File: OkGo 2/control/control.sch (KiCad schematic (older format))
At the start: 40 parts

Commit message: Specced/valued/footprinted a lot of parts
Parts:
- removed C?: CP, symbol CP
- removed C? (x2): C, symbol C
- removed U?: APE8865N-33-HF-3, SOT-23, symbol APE8865N-33-HF-3
- added C103, C104, C106, C114: 100n, Capacitors_SMD:C_0805_HandSoldering, symbol C
- added C113: 100u, Capacitors_SMD:C_1206_HandSoldering, symbol C
- added U101: ADP3335, Housings_SSOP:MSOP-8_3x3mm_Pitch0.65mm, symbol ADP3335
- C101, C102: renamed from C?; value C -> 2u2; footprint (none) -> Capacitors_SMD:C_0805_HandSoldering; Farnell (none) -> 2362106
- C105: renamed from C?; value 100n -> 4u7; footprint (none) -> Capacitors_SMD:C_0805_HandSoldering; Farnell (none) -> 1845742
- C107: renamed from C?; value C -> 100n; footprint (none) -> Capacitors_SMD:C_0805_HandSoldering; Farnell (none) -> 2407344
- C108: renamed from C?; value C -> 4u7; footprint (none) -> Capacitors_SMD:C_0805_HandSoldering; Farnell (none) -> 1845742
- C109: renamed from C?; value C -> 10n; footprint (none) -> Capacitors_SMD:C_0805_HandSoldering; Farnell (none) -> 2407341
- C110: renamed from C?; value C -> 1u; footprint (none) -> Capacitors_SMD:C_0805_HandSoldering; Farnell (none) -> 9227792
- C111, C112: renamed from C?; value C -> 15p; footprint (none) -> Capacitors_SMD:C_0805_HandSoldering; Farnell (none) -> 1414668
- R101: renamed from R?; value R -> 3k3; footprint (none) -> Resistors_SMD:R_0805_HandSoldering; Farnell (none) -> 9237682
- R102: renamed from R?; value R -> 10k; footprint (none) -> Capacitors_SMD:C_0805_HandSoldering; Farnell (none) -> 9237755
- R104, R106, R107, R108: renamed from R?; footprint (none) -> Resistors_SMD:R_0805_HandSoldering; Farnell (none) -> 2331808
- R105: renamed from R?; value R -> 100R; footprint (none) -> Resistors_SMD:R_0805_HandSoldering; Farnell (none) -> 2331783
- RV101: renamed from RV?; Farnell (none) -> 9354824
- U102: renamed from U?; footprint (none) -> common:FTSH-105-01-F-D-K
- U104: renamed from U?; footprint (none) -> Housings_QFP:LQFP-48_7x7mm_Pitch0.5mm; Farnell (none) -> 2432093
- Y101: renamed from Y?; value Crystal -> 8MHz; Farnell (none) -> 2101329
- gave numbers to parts that had none: 16
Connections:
- wire segments 130 -> 147
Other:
- moved on the sheet: C101, C102, D101, P101, R101, R102, R103, TP101, TP102, TP103

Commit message: Lots and lots of part selections and small mods
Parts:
- removed P102, P103, P104, P106: CONN_01X04, symbol CONN_01X04
- removed P105: ANT, symbol CONN_01X02
- removed R104, R106, R107, R108: 10k, Resistors_SMD:R_0805_HandSoldering, symbol R
- added BT?: LiPO_1S, symbol LiPO_1S
- added F?: FUSE, symbol FUSE
- added P?: SMA, common:SMA-142-0701-801, symbol SMA
- added P? (x2): BATT_CASE, symbol CONN_01X02
- added P?: BATT, symbol CONN_01X02
- added P?: BATT_JST_XH, symbol CONN_01X02
- added SW?: Latching Push, symbol SPST_small
- added U?: MEU1S0303ZC, symbol MEU1S0303ZC
- P101: value BATT_IN -> BATT
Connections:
- net labels added: +5V
- wire segments 147 -> 137
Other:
- moved on the sheet: C101, C102, C103, C104, C105, C106, C107, C108, C109, C110, C111, C112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

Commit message: New power buttons and arm/disarm LED
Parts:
- removed P101, P?: BATT, symbol CONN_01X02
- removed SW?: Latching Push, symbol SPST_small
- added D?: Led_x2, symbol Led_x2
- added P? (x2): KEYSW, symbol CONN_01X02
- added P? (x2): BATT, symbol CONN_01X02
- added R?: 10k, Resistors_SMD:R_0805_HandSoldering, symbol R
- added R? (x2): 68R, Resistors_SMD:R_0805_HandSoldering, symbol R
- added SW?: KEYSWITCH, symbol SPST_small
- added SW?: LATCHING PUSH, symbol SPST_small
- added U?: BEZEL, symbol PART
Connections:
- net labels added: +3.3V, ARM_LED, ARM_SW, DISARM_LED
- wire segments 137 -> 153
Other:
- note added: "GREEN: 2.1V 20mA"
- note added: "RED: 1.95V 20mA"
- moved on the sheet: BT?, D101, F?, P?, R101, R102, TP102, TP103

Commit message: Lots of footprinting.
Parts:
- removed D102: POWER, symbol LED
- removed R103: R, symbol R
- added U?: FUSE 1A, symbol PART
- BT101: renamed from BT?; URL (none) -> https://www.coolcomponents.co.uk/lithium-polymer-battery-20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
- F101: renamed from F?; value FUSE -> 5x20; footprint (none) -> control:5x20_clip; Farnell (none) -> 1162740
- RV101: footprint (none) -> control:bourns3386G
- U103: footprint (none) -> Pin_Headers:Pin_Header_Straight_1x16
- U105: footprint (none) -> common:RFM95W
- U106: renamed from U?; footprint (none) -> control:meu1
- Y101: footprint (none) -> common:XTAL50x32
- gave numbers to parts that had none: 15
- renumbered R102 to R103, R105 to R106, TP102 to TP101, TP101 to TP102, U102 to U107
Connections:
- wire segments 153 -> 151
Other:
- moved on the sheet: TP102

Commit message: Finished footprinting control, #7
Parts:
- added P108, P109: ARM_LED, symbol CONN_01X03
- D102: value Led_x2 -> RED/GREEN
- P103: footprint (none) -> common:JST-PA-2; Farnell (none) -> 1830747
- gave numbers to parts that had none: 1
- renumbered P108 to P110, U101 to U102, U102 to U103, U103 to U104, U104 to U105, U105 to U106, U106 to U107, U107 to U108
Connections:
- net GND: now also P108.1 (P1); no longer D102.2 (K)
- net at D102.1 (A1): now also P109.2 (P2); no longer R105.1
- net at D102.3 (A2): now also P109.3 (P3); no longer R104.1
- new net: D102.2 (K), P109.1 (P1)
- new net: P108.3 (P3), R104.1
- new net: P108.2 (P2), R105.1
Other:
- moved on the sheet: D102, R104, U103

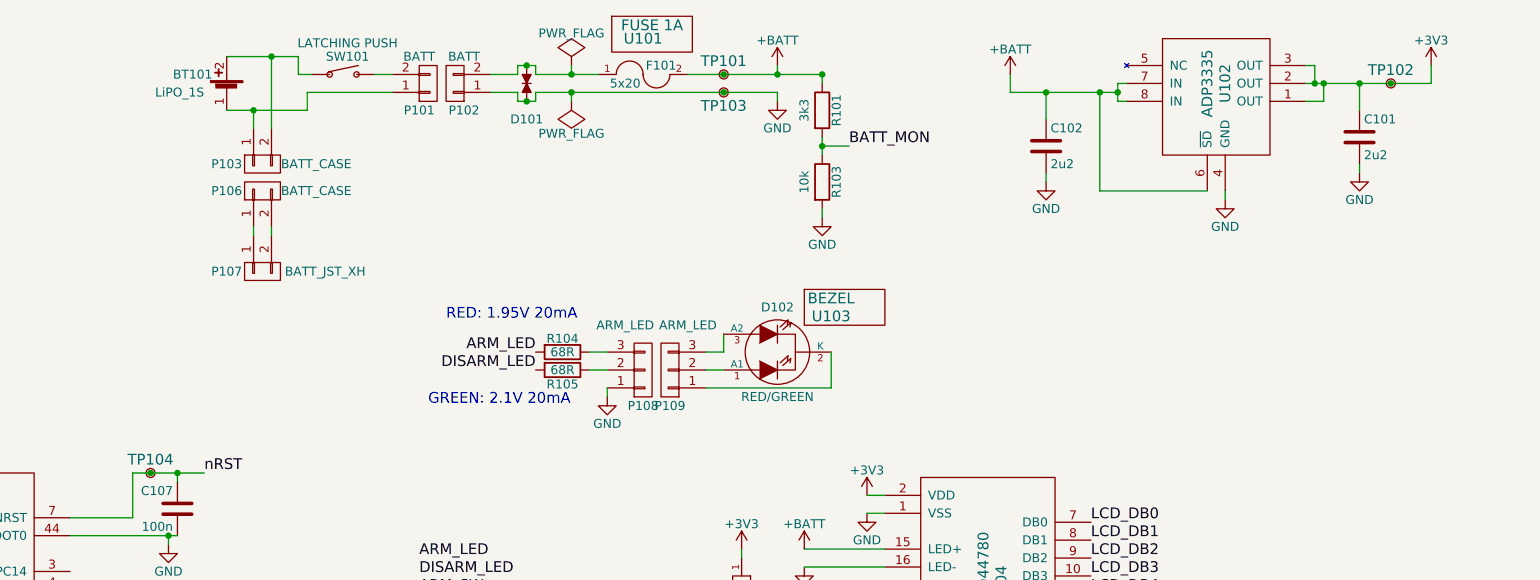
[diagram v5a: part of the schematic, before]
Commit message: Footprinting on ignition + TPs
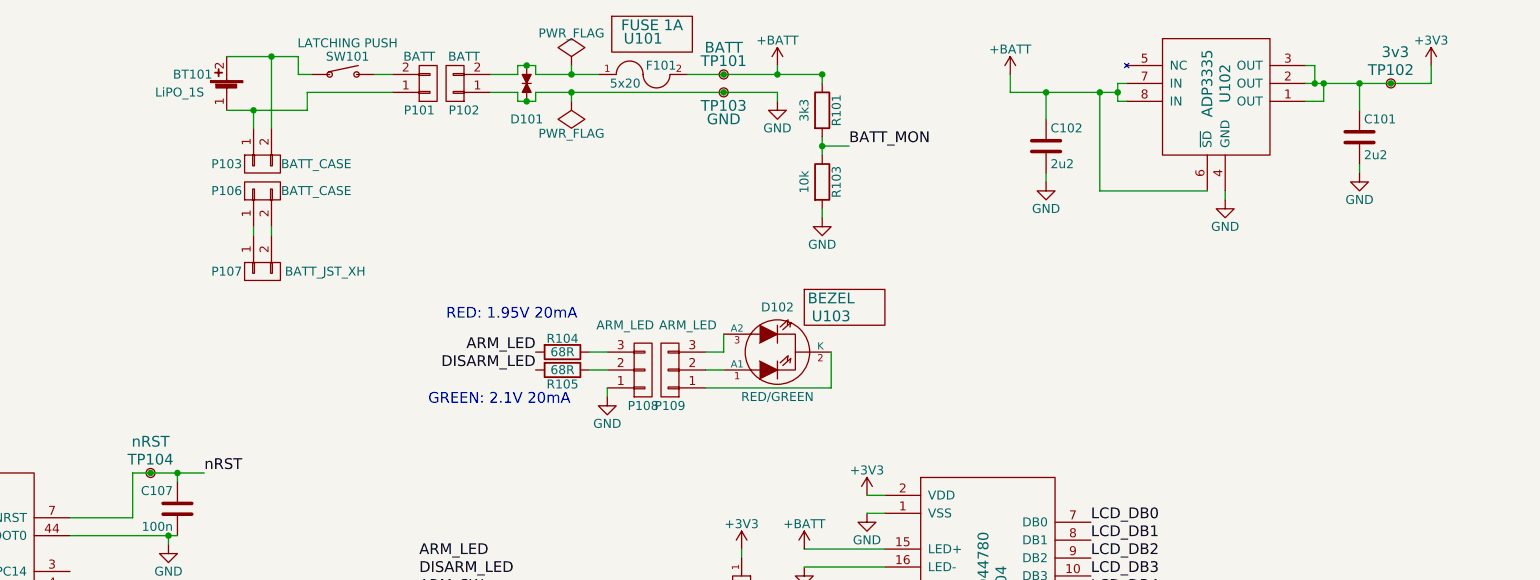
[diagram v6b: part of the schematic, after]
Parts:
- TP101: value TestPoint -> BATT; footprint (none) -> common:TESTPOINT
- TP102: value TestPoint -> 3v3; footprint (none) -> common:TESTPOINT
- TP103: value TestPoint -> GND; footprint (none) -> common:TESTPOINT
- TP104: value TestPoint -> nRST; footprint (none) -> common:TESTPOINT
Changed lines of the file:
@@
 P 10425 950
 F 0 "TP102" H 10425 875 60  0000 C CNN
-F 1 "TestPoint" H 10400 775 60  0001 C CNN
-F 2 "" H 10425 950 60  0000 C CNN
+F 1 "3v3" H 10400 775 60  0000 C CNN
+F 2 "common:TESTPOINT" H 10425 950 60  0001 C CNN
 F 3 "" H 10425 950 60  0000 C CNN
 	1    10425 950
@@
 P 6700 900
 F 0 "TP101" H 6700 825 60  0000 C CNN
-F 1 "TestPoint" H 6675 725 60  0001 C CNN
-F 2 "" H 6700 900 60  0000 C CNN
+F 1 "BATT" H 6700 750 60  0000 C CNN
+F 2 "common:TESTPOINT" H 6700 900 60  0001 C CNN
 F 3 "" H 6700 900 60  0000 C CNN
 	1    6700 900
@@
 P 6700 1000
 F 0 "TP103" H 6700 925 60  0000 C CNN
-F 1 "TestPoint" H 6675 825 60  0001 C CNN
-F 2 "" H 6700 1000 60  0000 C CNN
+F 1 "GND" H 6700 850 60  0000 C CNN
+F 2 "common:TESTPOINT" H 6700 1000 60  0001 C CNN
 F 3 "" H 6700 1000 60  0000 C CNN
 	1    6700 1000
@@
 P 3500 3125
 F 0 "TP104" H 3500 3050 60  0000 C CNN
-F 1 "TestPoint" H 3475 2950 60  0001 C CNN
-F 2 "" H 3500 3125 60  0000 C CNN
+F 1 "nRST" H 3500 2950 60  0000 C CNN
+F 2 "common:TESTPOINT" H 3500 3125 60  0001 C CNN
 F 3 "" H 3500 3125 60  0000 C CNN
 	1    3500 3125

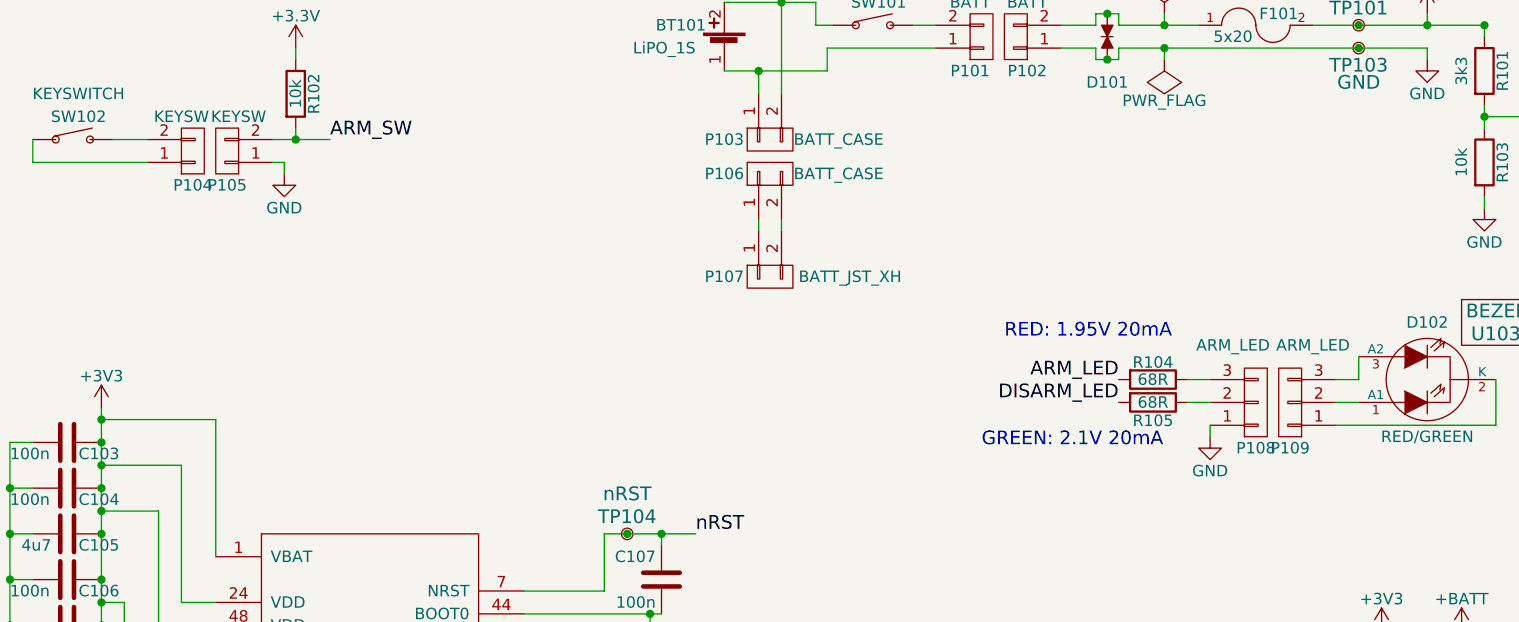
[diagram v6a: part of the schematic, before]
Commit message: Lots more footprinting, mostly done.
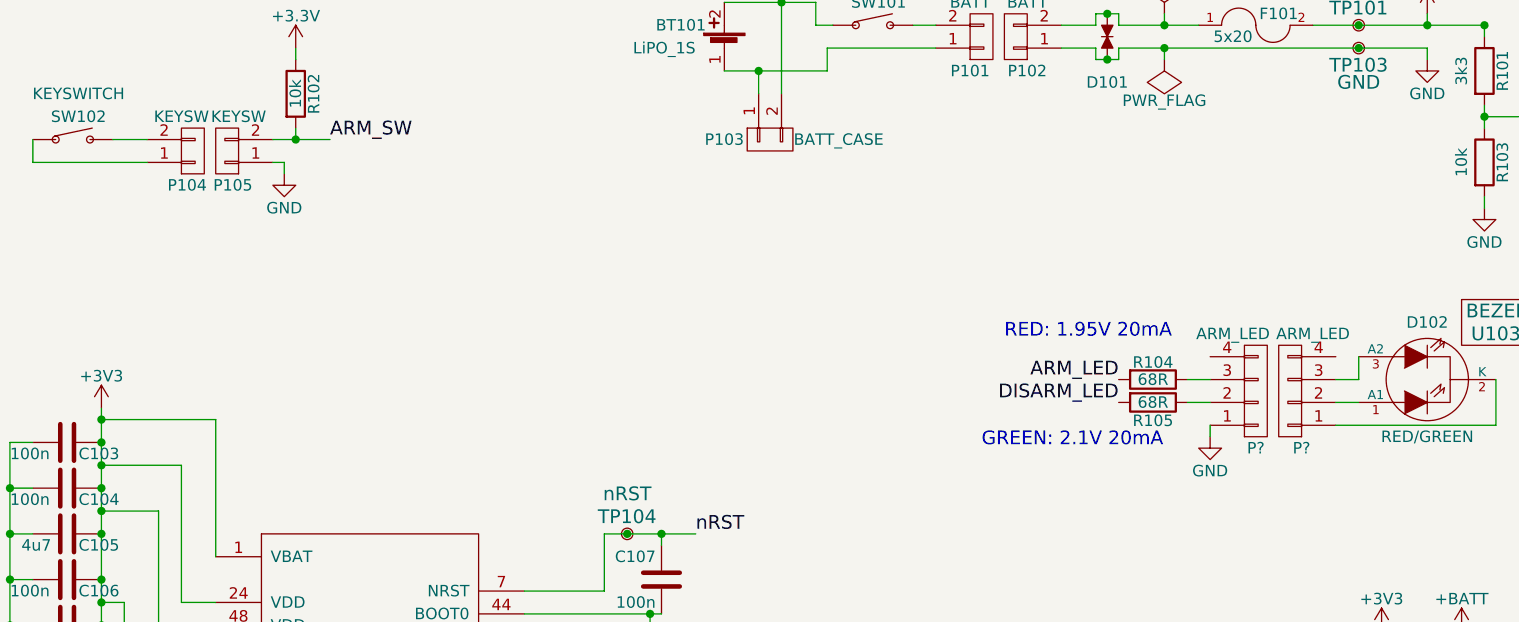
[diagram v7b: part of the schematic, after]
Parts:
- removed P106: BATT_CASE, symbol CONN_01X02
- removed P107: BATT_JST_XH, symbol CONN_01X02
- removed P108, P109: ARM_LED, symbol CONN_01X03
- added P?: ARM_LED, symbol CONN_01X04
- added P?: ARM_LED, common:JST-PA-4, symbol CONN_01X04
- P101, P104: Farnell (none) -> 1830726
- P102, P105: footprint (none) -> common:JST-PA-2; Farnell (none) -> 1830747
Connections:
- net GND: now also P?.1 (P1)
- net at D102.1 (A1): now also P?.2 (P2)
- net at D102.2 (K): now also P?.1 (P1)
- net at D102.3 (A2): now also P?.3 (P3)
- net at R104.1: now also P?.3 (P3)
- net at R105.1: now also P?.2 (P2)
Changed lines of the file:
@@
-$EndComp
-$Comp
-L CONN_01X02 P106
-U 1 1 55A21CFA
-P 4125 1550
-F 0 "P106" V 4125 1750 50  0000 C CNN
-F 1 "BATT_CASE" V 4125 1250 50  0000 C CNN
-F 2 "" H 4125 1550 60  0000 C CNN
-F 3 "" H 4125 1550 60  0000 C CNN
-	1    4125 1550
-	0    -1   -1   0
-$EndComp
-$Comp
-L CONN_01X02 P107
-U 1 1 55A2205A
-P 4125 2000
-F 0 "P107" V 4125 2200 50  0000 C CNN
-F 1 "BATT_JST_XH" V 4125 1650 50  0000 C CNN
-F 2 "" H 4125 2000 60  0000 C CNN
-F 3 "" H 4125 2000 60  0000 C CNN
-	1    4125 2000
-	0    -1   1    0
 $EndComp
 $Comp
@@
 U 1 1 55A7FC01
 P 1600 1450
-F 0 "P104" H 1600 1600 50  0000 C CNN
+F 0 "P104" H 1575 1600 50  0000 C CNN
 F 1 "KEYSW" H 1550 1300 50  0000 C CNN
 F 2 "" H 1600 1450 60  0000 C CNN
 F 3 "" H 1600 1450 60  0000 C CNN
+F 4 "1830726" H 1600 1450 60  0001 C CNN "Farnell"
 	1    1600 1450
 	1    0    0    1
@@
 U 1 1 55A7FE33
 P 1750 1450
-F 0 "P105" H 1750 1600 50  0000 C CNN
+F 0 "P105" H 1725 1600 50  0000 C CNN
 F 1 "KEYSW" H 1700 1300 50  0000 C CNN
-F 2 "" H 1750 1450 60  0000 C CNN
+F 2 "common:JST-PA-2" H 1750 1450 60  0001 C CNN
 F 3 "" H 1750 1450 60  0000 C CNN
+F 4 "1830747" H 1750 1450 60  0001 C CNN "Farnell"
 	1    1750 1450
 	-1   0    0    1
@@
 Connection ~ 4075 1100
 Wire Wire Line
-	4075 1750 4075 1800
-Wire Wire Line
-	4175 1800 4175 1750
-Wire Wire Line
 	5650 900  6000 900
 Wire Wire Line
@@
 F 0 "P102" H 5150 1100 50  0000 C CNN
 F 1 "BATT" H 5150 800 50  0000 C CNN
-F 2 "" H 5200 950 60  0000 C CNN
+F 2 "common:JST-PA-2" H 5200 950 60  0001 C CNN
 F 3 "" H 5200 950 60  0000 C CNN
+F 4 "1830747" H 5200 950 60  0001 C CNN "Farnell"
 	1    5200 950
 	-1   0    0    1
@@
 F 2 "" H 5050 950 60  0000 C CNN
 F 3 "" H 5050 950 60  0000 C CNN
+F 4 "1830726" H 5050 950 60  0001 C CNN "Farnell"
 	1    5050 950
 	1    0    0    1
@@
 Wire Wire Line
 	6700 2450 6700 2350
-$Comp
-L CONN_01X03 P108
-U 1 1 55AA7717
-P 6250 2550
-F 0 "P108" H 6250 2750 50  0000 C CNN
-F 1 "ARM_LED" H 6150 2300 50  0000 C CNN
-F 2 "" H 6250 2550 60  0000 C CNN
-F 3 "" H 6250 2550 60  0000 C CNN
-	1    6250 2550
-	1    0    0    1
-$EndComp
-$Comp
-L CONN_01X03 P109
-U 1 1 55AA784F
-P 6400 2550
-F 0 "P109" H 6400 2750 50  0000 C CNN
-F 1 "ARM_LED" H 6300 2300 50  0000 C CNN
-F 2 "" H 6400 2550 60  0000 C CNN
-F 3 "" H 6400 2550 60  0000 C CNN
-	1    6400 2550
-	-1   0    0    1
-$EndComp
 Wire Wire Line
 	5950 2450 6050 2450
@@
 Wire Wire Line
 	7300 2650 6600 2650
+$Comp
+L CONN_01X04 P?
+U 1 1 55AB5A44
+P 6400 2500
+F 0 "P?" H 6350 2750 50  0000 C CNN
+F 1 "ARM_LED" H 6300 2250 50  0000 C CNN
+F 2 "" H 6400 2500 60  0000 C CNN
+F 3 "" H 6400 2500 60  0000 C CNN
+F 4 "1830729" H 6400 2500 60  0001 C CNN "Farnell"
+	1    6400 2500
+	-1   0    0    1
+$EndComp
+$Comp
+L CONN_01X04 P?
+U 1 1 55AB5EAE
+P 6250 2500
+F 0 "P?" H 6250 2750 50  0000 C CNN
+F 1 "ARM_LED" H 6150 2250 50  0000 C CNN
+F 2 "common:JST-PA-4" H 6250 2500 60  0001 C CNN
+F 3 "" H 6250 2500 60  0000 C CNN
+F 4 "1830749" H 6250 2500 60  0001 C CNN "Farnell"
+	1    6250 2500
+	1    0    0    1
+$EndComp
 $EndSCHEMATC
